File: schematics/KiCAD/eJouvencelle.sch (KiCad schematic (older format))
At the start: 44 parts

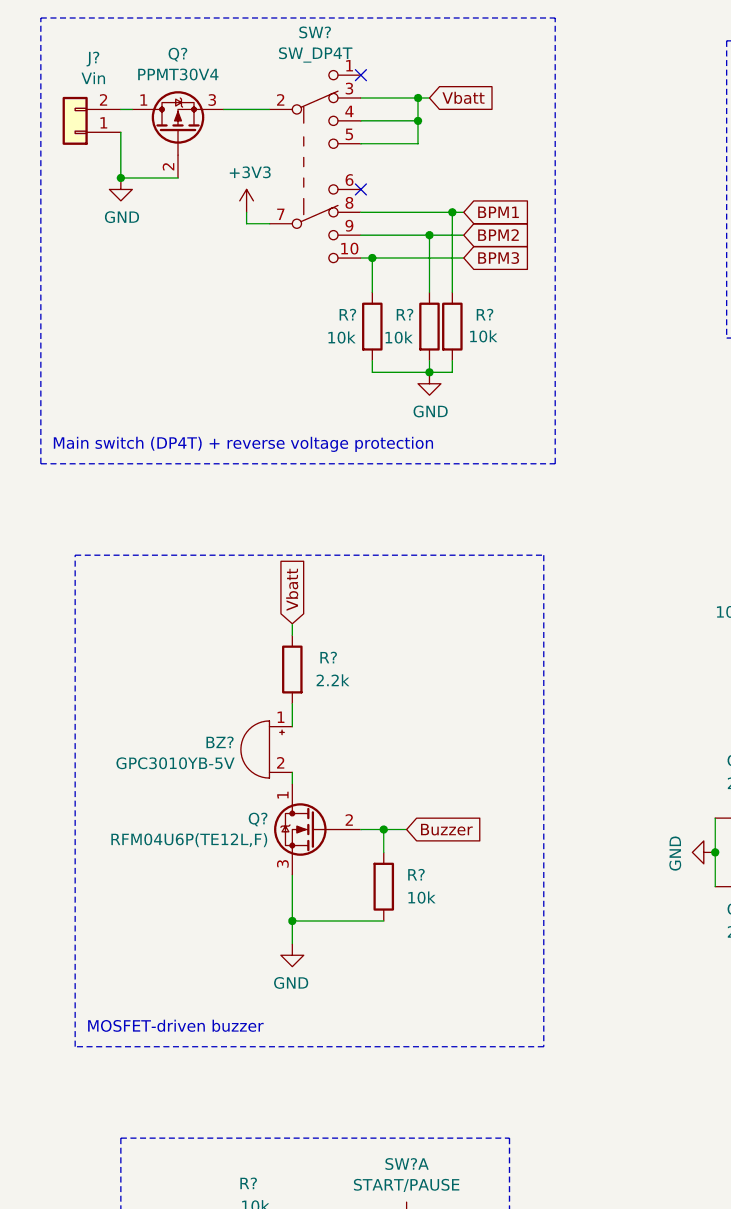
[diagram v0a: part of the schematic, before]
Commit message: include TC4428 in kicad schematics
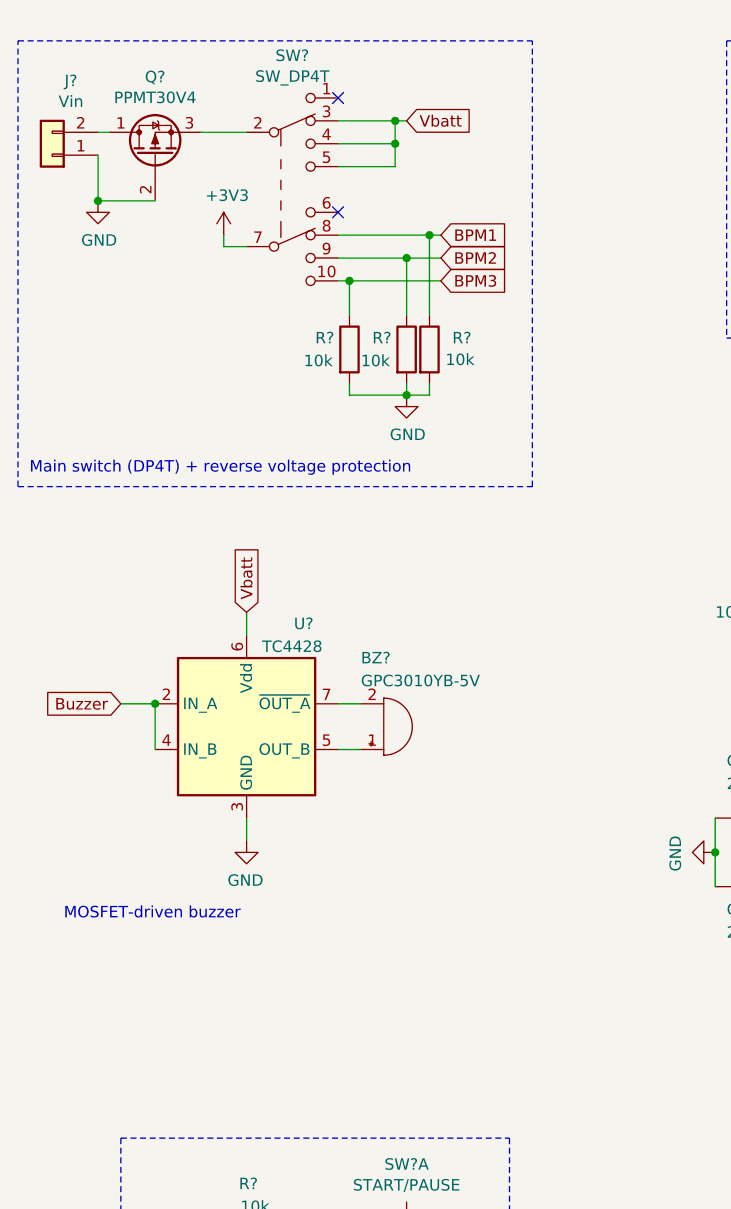
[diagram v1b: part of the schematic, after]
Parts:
- removed Q?: RFM04U6P(TE12L,F), symbol Device:Q_NMOS_DGS
- removed R?: 2.2k, symbol Device:R
- removed R?: 10k, symbol Device:R
- added U?: TC4428, Package_SO:MSOP-8_3x3mm_P0.65mm, symbol eJouvencelle:TC4428
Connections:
- net Buzzer: now also U?.2 (IN_A), U?.4 (IN_B)
- net GND: now also U?.3 (GND)
- net Vbatt: now also U?.6 (Vdd)
- net at BZ?.1 (-): now also U?.5 (OUT_B)
- net at BZ?.2 (+): now also U?.7 (~OUT_A)
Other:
- moved on the sheet: BZ?, J?, Q?, R?, SW?

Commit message: Update eJouvencelle.sch
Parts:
- added C?: 470uF, symbol Device:CP_Small
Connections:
- net GND: now also C?.2
- net Vbatt: now also C?.1
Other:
- note added: "Buzzer"
- note removed: "MOSFET-driven buzzer"
- moved on the sheet: BZ?, U?
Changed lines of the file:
@@
 Text Notes 7800 3100 0    50   ~ 0
 7-segment w/ BCD decoder
-Text GLabel 2000 3250 1    50   Input ~ 0
+Text GLabel 2100 3450 1    50   Input ~ 0
 Vbatt
-Text GLabel 1450 3650 0    50   Input ~ 0
+Text GLabel 1550 4050 0    50   Input ~ 0
 Buzzer
-Text Notes 1200 4600 0    50   ~ 0
-MOSFET-driven buzzer
+Text Notes 1300 4950 0    50   ~ 0
+Buzzer
 Text GLabel 4550 5150 0    50   Input ~ 0
 Buzzer
@@
 L power:GND #PWR?
 U 1 1 5EA2FE7F
-P 2000 4250
-F 0 "#PWR?" H 2000 4000 50  0001 C CNN
-F 1 "GND" H 2005 4077 50  0000 C CNN
-F 2 "" H 2000 4250 50  0001 C CNN
-F 3 "" H 2000 4250 50  0001 C CNN
-	1    2000 4250
+P 2100 4650
+F 0 "#PWR?" H 2100 4400 50  0001 C CNN
+F 1 "GND" H 2105 4477 50  0000 C CNN
+F 2 "" H 2100 4650 50  0001 C CNN
+F 3 "" H 2100 4650 50  0001 C CNN
+	1    2100 4650
 	-1   0    0    -1
 $EndComp
@@
 L Device:Buzzer BZ?
 U 1 1 5E9C10D5
-P 2600 3750
-F 0 "BZ?" H 2500 3450 50  0000 L CNN
-F 1 "GPC3010YB-5V" H 2500 3550 50  0000 L CNN
-F 2 "" V 2575 3850 50  0001 C CNN
-F 3 "~" V 2575 3850 50  0001 C CNN
-	1    2600 3750
+P 2700 4150
+F 0 "BZ?" H 2600 3850 50  0000 L CNN
+F 1 "GPC3010YB-5V" H 2600 3950 50  0000 L CNN
+F 2 "" V 2675 4250 50  0001 C CNN
+F 3 "~" V 2675 4250 50  0001 C CNN
+	1    2700 4150
 	1    0    0    1
 $EndComp
@@
 Wire Wire Line
 	5100 2800 5100 2850
+Wire Wire Line
+	1700 4050 1700 4250
+Wire Wire Line
+	1550 4050 1700 4050
+Wire Wire Line
+	2500 4050 2600 4050
+Wire Wire Line
+	2500 4250 2600 4250
+Wire Wire Line
+	2100 4550 2100 4650
+$Comp
+L power:GND #PWR?
+U 1 1 60E9B367
+P 1550 3750
+F 0 "#PWR?" H 1550 3500 50  0001 C CNN
+F 1 "GND" H 1555 3577 50  0000 C CNN
+F 2 "" H 1550 3750 50  0001 C CNN
+F 3 "" H 1550 3750 50  0001 C CNN
+	1    1550 3750
+	-1   0    0    -1
+$EndComp
+Wire Wire Line
+	2100 3450 2100 3550
+Connection ~ 2100 3550
+Wire Wire Line
+	2100 3550 2100 3750
+Connection ~ 1700 4050
 $Comp
 L eJouvencelle:TC4428 U?
 U 1 1 60E78FEB
-P 2000 3750
-F 0 "U?" H 2250 4200 50  0000 C CNN
-F 1 "TC4428" H 2200 4100 50  0000 C CNN
-F 2 "Package_SO:MSOP-8_3x3mm_P0.65mm" H 1950 3250 50  0001 C CNN
-F 3 "http://ww1.microchip.com/downloads/en/devicedoc/hv9967b.pdf" H 2000 3750 50  0001 C CNN
-	1    2000 3750
-	1    0    0    -1
-$EndComp
-Wire Wire Line
-	1600 3650 1600 3850
-Wire Wire Line
-	1450 3650 1600 3650
-Connection ~ 1600 3650
-Wire Wire Line
-	2400 3650 2500 3650
-Wire Wire Line
-	2400 3850 2500 3850
-Wire Wire Line
-	2000 3250 2000 3350
-Wire Wire Line
-	2000 4150 2000 4250
+P 2100 4150
+F 0 "U?" H 2350 4600 50  0000 C CNN
+F 1 "TC4428" H 2300 4500 50  0000 C CNN
+F 2 "Package_SO:MSOP-8_3x3mm_P0.65mm" H 2050 3650 50  0001 C CNN
+F 3 "http://ww1.microchip.com/downloads/en/devicedoc/hv9967b.pdf" H 2100 4150 50  0001 C CNN
+	1    2100 4150
+	1    0    0    -1
+$EndComp
+$Comp
+L Device:CP_Small C?
+U 1 1 60E925D2
+P 1550 3650
+F 0 "C?" H 1638 3696 50  0000 L CNN
+F 1 "470uF" H 1638 3605 50  0000 L CNN
+F 2 "" H 1550 3650 50  0001 C CNN
+F 3 "~" H 1550 3650 50  0001 C CNN
+	1    1550 3650
+	1    0    0    -1
+$EndComp
+Wire Wire Line
+	1550 3550 2100 3550
+Wire Notes Line
+	1150 3100 3300 3100
+Wire Notes Line
+	3300 3100 3300 5000
+Wire Notes Line
+	3300 5000 1150 5000
+Wire Notes Line
+	1150 5000 1150 3100
 $EndSCHEMATC

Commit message: change CD4511 for SMD model
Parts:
- U?: value CD4511 -> CD4511BPW; footprint (none) -> Package_SO:TSSOP-16_4.4x5mm_P0.65mm
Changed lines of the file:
@@
 P 8550 2050
 F 0 "U?" H 8300 2600 50  0000 C CNN
-F 1 "CD4511" H 8350 2500 50  0000 C CNN
-F 2 "" H 8550 2050 50  0001 C CNN
+F 1 "CD4511BPW" H 8350 2500 50  0000 C CNN
+F 2 "Package_SO:TSSOP-16_4.4x5mm_P0.65mm" H 8550 2050 50  0001 C CNN
 F 3 "http://www.ti.com/lit/ds/symlink/cd4543b.pdf" H 8550 2050 50  0001 C CNN
 	1    8550 2050

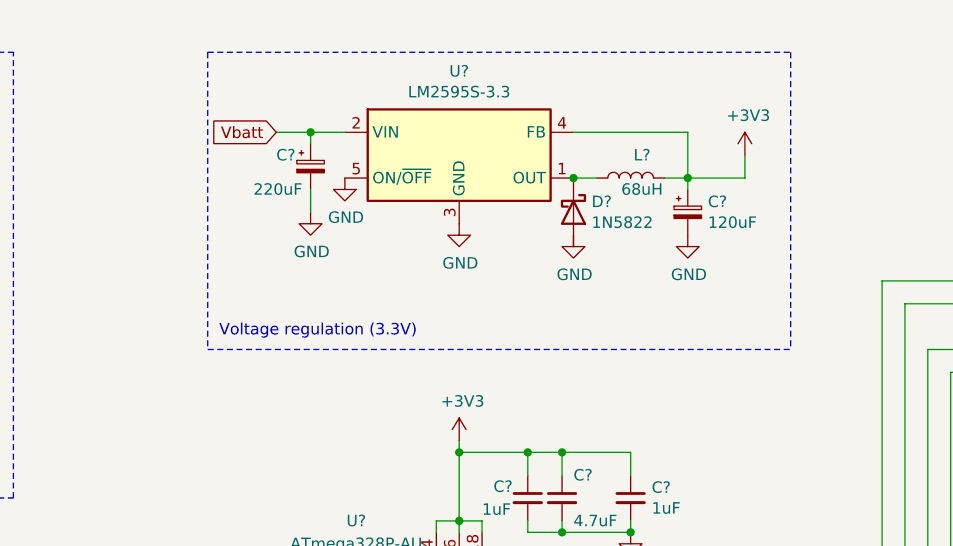
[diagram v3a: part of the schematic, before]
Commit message: add footprints + switch buck converter type
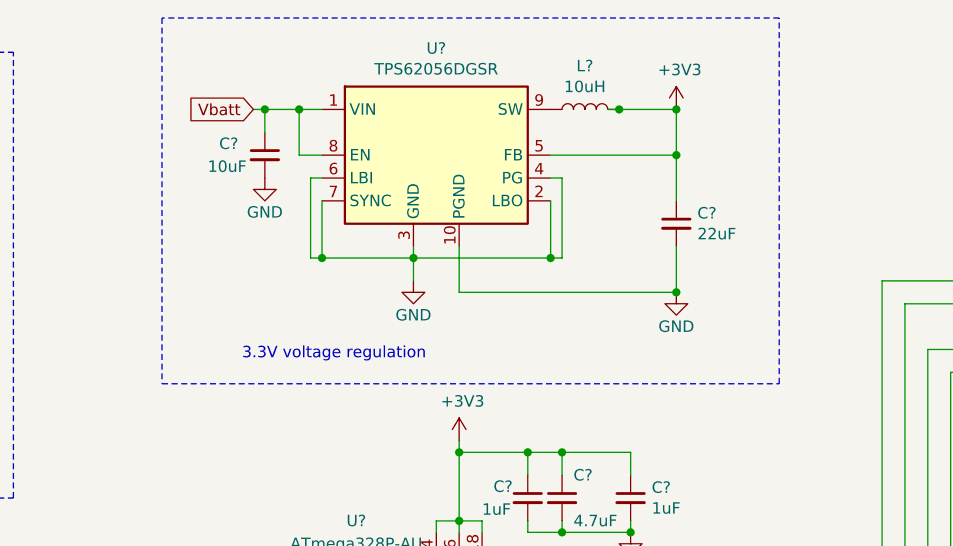
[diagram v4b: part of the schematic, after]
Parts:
- removed C?: 220uF, symbol Device:CP_Small
- removed C?: 120uF, symbol Device:CP_Small
- removed D?: 1N5822, Diode_THT:D_DO-201AD_P15.24mm_Horizontal, symbol Diode:1N5822
- removed L?: 68uH, symbol Device:L
- removed U?: LM2595S-3.3, Package_TO_SOT_SMD:TO-263-5_TabPin3, symbol Regulator_Switching:LM2595S-3.3
- added C?: 10uF, Capacitor_SMD:C_0603_1608Metric, symbol Device:C_Small
- added C?: 22uF, Capacitor_SMD:C_0603_1608Metric, symbol Device:C_Small
- added L?: 10uH, Inductor_SMD:L_0805_2012Metric, symbol Device:L
- added U?: TPS62056DGSR, Package_SO:VSSOP-10_3x3mm_P0.5mm, symbol Regulator_Switching:TPS62056DGS
- C? (x10): footprint (none) -> Capacitor_SMD:C_0603_1608Metric
- C?: footprint (none) -> Capacitor_Tantalum_SMD:CP_EIA-7343-15_Kemet-W
- Q?: footprint (none) -> Package_TO_SOT_SMD:SOT-23
- R? (x15): footprint (none) -> Resistor_SMD:R_0603_1608Metric
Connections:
- net +3V3: now also C?.1, L?.2, U?.5 (FB)
- net GND: now also C?.2, C?.2, U?.10 (PGND), U?.2 (LBO), U?.3 (GND), U?.4 (PG), U?.6 (LBI), U?.7 (SYNC)
- net Vbatt: now also C?.1, U?.1 (VIN), U?.8 (EN)
- new net: L?.1, U?.9 (SW)
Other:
- note added: "3.3V voltage regulation"
- note removed: "Voltage regulation (3.3V)"

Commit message: add footprints to the SFPI header
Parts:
- J?: footprint (none) -> Connector_PinHeader_1.00mm:PinHeader_1x06_P1.00mm_Vertical
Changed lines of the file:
@@
 F 0 "J?" H 9542 4625 50  0000 C CNN
 F 1 "1X6 female header" H 9650 4700 50  0000 C CNN
-F 2 "" H 9650 5150 50  0001 C CNN
+F 2 "Connector_PinHeader_1.00mm:PinHeader_1x06_P1.00mm_Vertical" H 9650 5150 50  0001 C CNN
 F 3 "~" H 9650 5150 50  0001 C CNN
 	1    9650 5150
